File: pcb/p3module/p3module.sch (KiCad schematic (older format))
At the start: 38 parts, among them J1 Conn_01x08_Female, J2 Conn_02x10_Counter_Clockwise, J3 Conn_01x08_Female, U1 74HC595, U2 74HC165, U3 74HC595, U4 4051

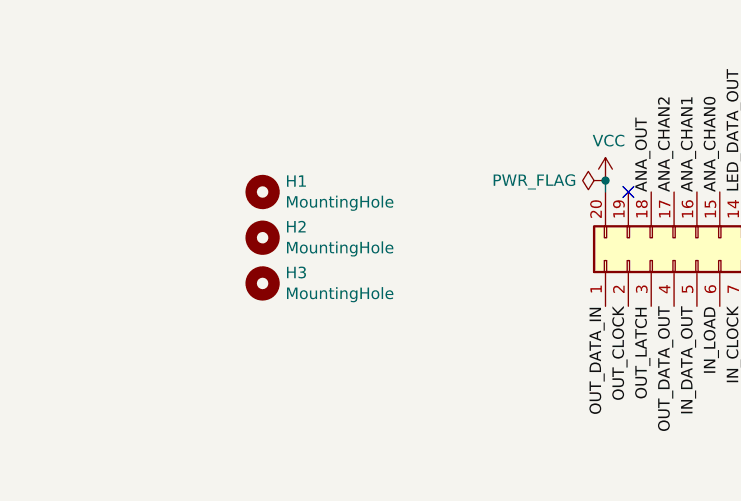
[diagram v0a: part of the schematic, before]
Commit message: reduced height to 10cm
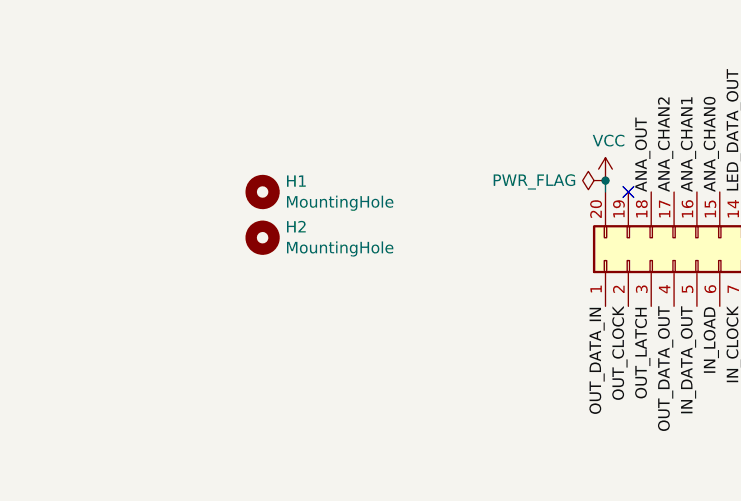
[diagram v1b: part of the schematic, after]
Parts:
- removed H3: MountingHole, MountingHole:MountingHole_3.2mm_M3, symbol Mechanical:MountingHole
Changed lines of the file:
@@
-$EndComp
-$Comp
-L Mechanical:MountingHole H3
-U 1 1 60272F90
-P 2650 5750
-F 0 "H3" H 2750 5796 50  0000 L CNN
-F 1 "MountingHole" H 2750 5705 50  0000 L CNN
-F 2 "MountingHole:MountingHole_3.2mm_M3" H 2650 5750 50  0001 C CNN
-F 3 "~" H 2650 5750 50  0001 C CNN
-	1    2650 5750
-	1    0    0    -1
 $EndComp
 $Comp

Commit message: another attempt at routing
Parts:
- removed J2: Conn_02x10_Counter_Clockwise, Connector_PinHeader_2.54mm:PinHeader_2x10_P2.54mm_Vertical, symbol Connector_Generic:Conn_02x10_Counter_Clockwise
- added J2: Conn_02x10_Odd_Even, Connector_PinHeader_2.54mm:PinHeader_1x20_P2.54mm_Vertical, symbol Connector_Generic:Conn_02x10_Odd_Even
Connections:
- net ANA_CHAN0: now also J2.12 (Pin_12)
- net ANA_CHAN1: now also J2.10 (Pin_10)
- net ANA_CHAN2: now also J2.8 (Pin_8)
- net ANA_OUT: now also J2.6 (Pin_6)
- net GND: now also J2.19 (Pin_19)
- net IN_CLOCK: now also J2.13 (Pin_13)
- net IN_CLOCK_ENABLE: now also J2.15 (Pin_15)
- net IN_DATA_IN: now also J2.17 (Pin_17)
- net IN_DATA_OUT: now also J2.9 (Pin_9)
- net IN_LOAD: now also J2.11 (Pin_11)
- net LED_CLOCK: now also J2.18 (Pin_18)
- net LED_DATA_IN: now also J2.20 (Pin_20)
- net LED_DATA_OUT: now also J2.14 (Pin_14)
- net LED_LATCH: now also J2.16 (Pin_16)
- net OUT_CLOCK: now also J2.3 (Pin_3)
- net OUT_DATA_IN: now also J2.1 (Pin_1)
- net OUT_DATA_OUT: now also J2.7 (Pin_7)
- net OUT_LATCH: now also J2.5 (Pin_5)
- net VCC: now also J2.2 (Pin_2)
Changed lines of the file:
@@
 	8800 2950 8800 3000
 Connection ~ 8800 3000
-$Comp
-L Connector_Generic:Conn_02x10_Counter_Clockwise J2
-U 1 1 6027F5D1
-P 4550 5650
-F 0 "J2" V 4646 5062 50  0000 R CNN
-F 1 "Conn_02x10_Counter_Clockwise" V 4555 5062 50  0000 R CNN
-F 2 "Connector_PinHeader_2.54mm:PinHeader_2x10_P2.54mm_Vertical" H 4550 5650 50  0001 C CNN
-F 3 "~" H 4550 5650 50  0001 C CNN
-	1    4550 5650
-	0    -1   -1   0
-$EndComp
 Text Label 2150 2000 2    50   ~ 0
 OUT_DATA_IN
@@
 $EndComp
 Connection ~ 2550 3100
+$Comp
+L Connector_Generic:Conn_02x10_Odd_Even J2
+U 1 1 6029A9C2
+P 4550 5650
+F 0 "J2" V 4646 5062 50  0000 R CNN
+F 1 "Conn_02x10_Odd_Even" V 4555 5062 50  0000 R CNN
+F 2 "Connector_PinHeader_2.54mm:PinHeader_1x20_P2.54mm_Vertical" H 4550 5650 50  0001 C CNN
+F 3 "~" H 4550 5650 50  0001 C CNN
+	1    4550 5650
+	0    -1   -1   0
+$EndComp
 $EndSCHEMATC

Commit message: routing worked but one of the sockets was on the wrong side. ugh
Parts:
- J2: footprint Connector_PinHeader_2.54mm:PinHeader_1x20_P2.54mm_Vertical -> Connector_PinHeader_2.54mm:PinHeader_2x10_P2.54mm_Vertical
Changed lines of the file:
@@
 F 0 "J2" V 4646 5062 50  0000 R CNN
 F 1 "Conn_02x10_Odd_Even" V 4555 5062 50  0000 R CNN
-F 2 "Connector_PinHeader_2.54mm:PinHeader_1x20_P2.54mm_Vertical" H 4550 5650 50  0001 C CNN
+F 2 "Connector_PinHeader_2.54mm:PinHeader_2x10_P2.54mm_Vertical" H 4550 5650 50  0001 C CNN
 F 3 "~" H 4550 5650 50  0001 C CNN
 	1    4550 5650
